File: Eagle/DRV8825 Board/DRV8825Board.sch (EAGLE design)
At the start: 10 parts, among them X1 22-23-2031, X2 22-23-2041, X3 22-23-2041

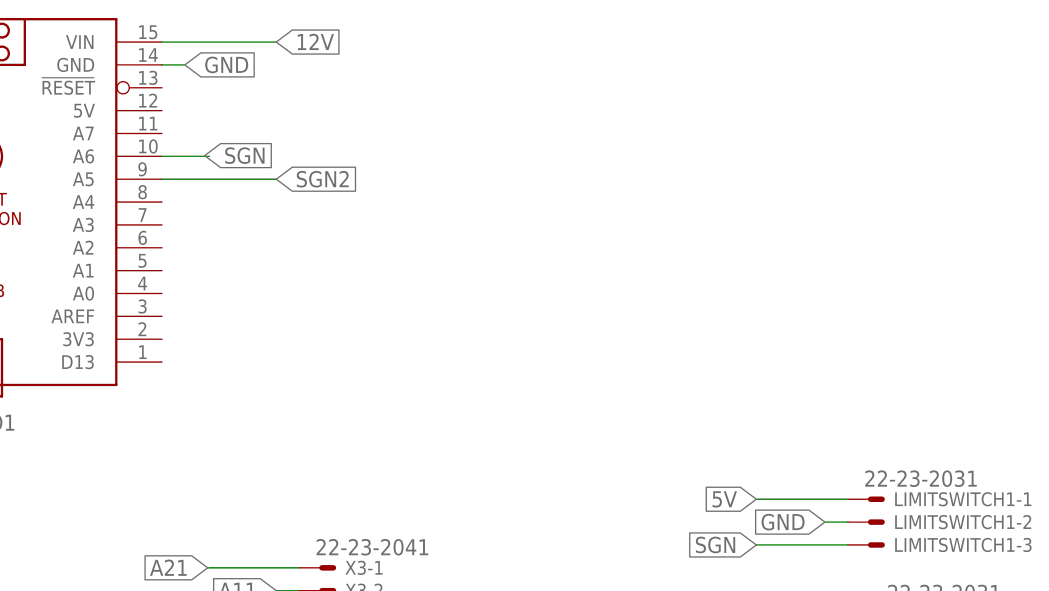
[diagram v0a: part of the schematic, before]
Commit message: Added a fan controller circuit
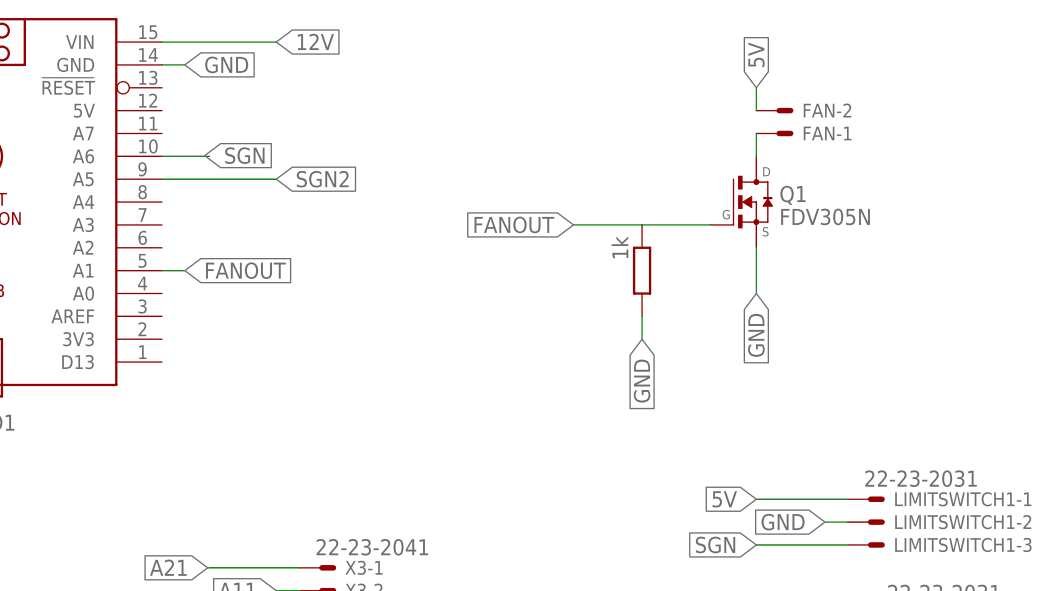
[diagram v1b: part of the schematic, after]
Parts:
- added FAN: 22-23-2021, con-molex:22-23-2021
- added Q1: FDV305N, FDV305N:FDV305N
- added R1: 1k, rcl:R-EU_R1206
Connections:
- new net FANOUT: ARDUINO_NANO1.A1, Q1.G, R1.1
- new net N$1: FAN-1.S, Q1.D
- net 5V: now also FAN-2.S
- net GND: now also Q1.S, R1.2
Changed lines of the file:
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@@
 <part name="C2" library="rcl" library_urn="urn:adsk.eagle:library:334" deviceset="CPOL-EU" device="E2.5-6" package3d_urn="urn:adsk.eagle:package:23349/1"/>
 <part name="X2" library="con-molex" library_urn="urn:adsk.eagle:library:165" deviceset="22-23-2041" device="" package3d_urn="urn:adsk.eagle:package:8078635/1"/>
+<part name="Q1" library="FDV305N" deviceset="FDV305N" device=""/>
+<part name="FAN" library="con-molex" library_urn="urn:adsk.eagle:library:165" deviceset="22-23-2021" device="" package3d_urn="urn:adsk.eagle:package:8078633/1"/>
+<part name="R1" library="rcl" library_urn="urn:adsk.eagle:library:334" deviceset="R-EU_" device="R1206" package3d_urn="urn:adsk.eagle:package:23540/2" value="1k"/>
 </parts>
 <sheets>
@@
 <attribute name="NAME" x="38.1" y="42.418" size="1.524" layer="95"/>
 </instance>
+<instance part="Q1" gate="G$1" x="83.82" y="139.7" smashed="yes">
+<attribute name="VALUE" x="86.36128125" y="137.15871875" size="1.778890625" layer="96"/>
+<attribute name="NAME" x="86.36438125" y="139.7" size="1.781059375" layer="95"/>
+</instance>
+<instance part="FAN" gate="-1" x="86.36" y="147.32" smashed="yes">
+<attribute name="NAME" x="88.9" y="146.558" size="1.524" layer="95"/>
+</instance>
+<instance part="FAN" gate="-2" x="86.36" y="149.86" smashed="yes">
+<attribute name="NAME" x="88.9" y="149.098" size="1.524" layer="95"/>
+</instance>
+<instance part="R1" gate="G$1" x="71.12" y="132.08" smashed="yes" rot="R270">
+<attribute name="VALUE" x="67.818" y="135.89" size="1.778" layer="96" rot="R270"/>
+</instance>
 </instances>
 <busses>
@@
 <wire x1="-68.58" y1="101.6" x2="-88.9" y2="101.6" width="0.1524" layer="91"/>
 <label x="-88.9" y="101.6" size="1.778" layer="95" rot="R180" xref="yes"/>
+</segment>
+<segment>
+<pinref part="FAN" gate="-2" pin="S"/>
+<wire x1="83.82" y1="149.86" x2="83.82" y2="152.4" width="0.1524" layer="91"/>
+<label x="83.82" y="152.4" size="1.778" layer="95" rot="R90" xref="yes"/>
 </segment>
 </net>
@@
 <wire x1="-12.7" y1="43.18" x2="-12.7" y2="33.02" width="0.1524" layer="91"/>
 </segment>
+<segment>
+<pinref part="Q1" gate="G$1" pin="S"/>
+<wire x1="83.82" y1="134.62" x2="83.82" y2="129.54" width="0.1524" layer="91"/>
+<label x="83.82" y="129.54" size="1.778" layer="95" rot="R270" xref="yes"/>
+</segment>
+<segment>
+<pinref part="R1" gate="G$1" pin="2"/>
+<wire x1="71.12" y1="127" x2="71.12" y2="124.46" width="0.1524" layer="91"/>
+<label x="71.12" y="124.46" size="1.778" layer="95" rot="R270" xref="yes"/>
+</segment>
 </net>
 <net name="12V" class="0">
@@
 </segment>
 </net>
+<net name="FANOUT" class="0">
+<segment>
+<pinref part="Q1" gate="G$1" pin="G"/>
+<pinref part="R1" gate="G$1" pin="1"/>
+<wire x1="78.74" y1="137.16" x2="71.12" y2="137.16" width="0.1524" layer="91"/>
+<wire x1="71.12" y1="137.16" x2="63.5" y2="137.16" width="0.1524" layer="91"/>
+<label x="63.5" y="137.16" size="1.778" layer="95" rot="R180" xref="yes"/>
+</segment>
+<segment>
+<pinref part="ARDUINO_NANO1" gate="G$1" pin="A1"/>
+<wire x1="17.78" y1="132.08" x2="20.32" y2="132.08" width="0.1524" layer="91"/>
+<label x="20.32" y="132.08" size="1.778" layer="95" xref="yes"/>
+</segment>
+</net>
+<net name="N$1" class="0">
+<segment>
+<pinref part="FAN" gate="-1" pin="S"/>
+<pinref part="Q1" gate="G$1" pin="D"/>
+<wire x1="83.82" y1="147.32" x2="83.82" y2="144.78" width="0.1524" layer="91"/>
+</segment>
+</net>

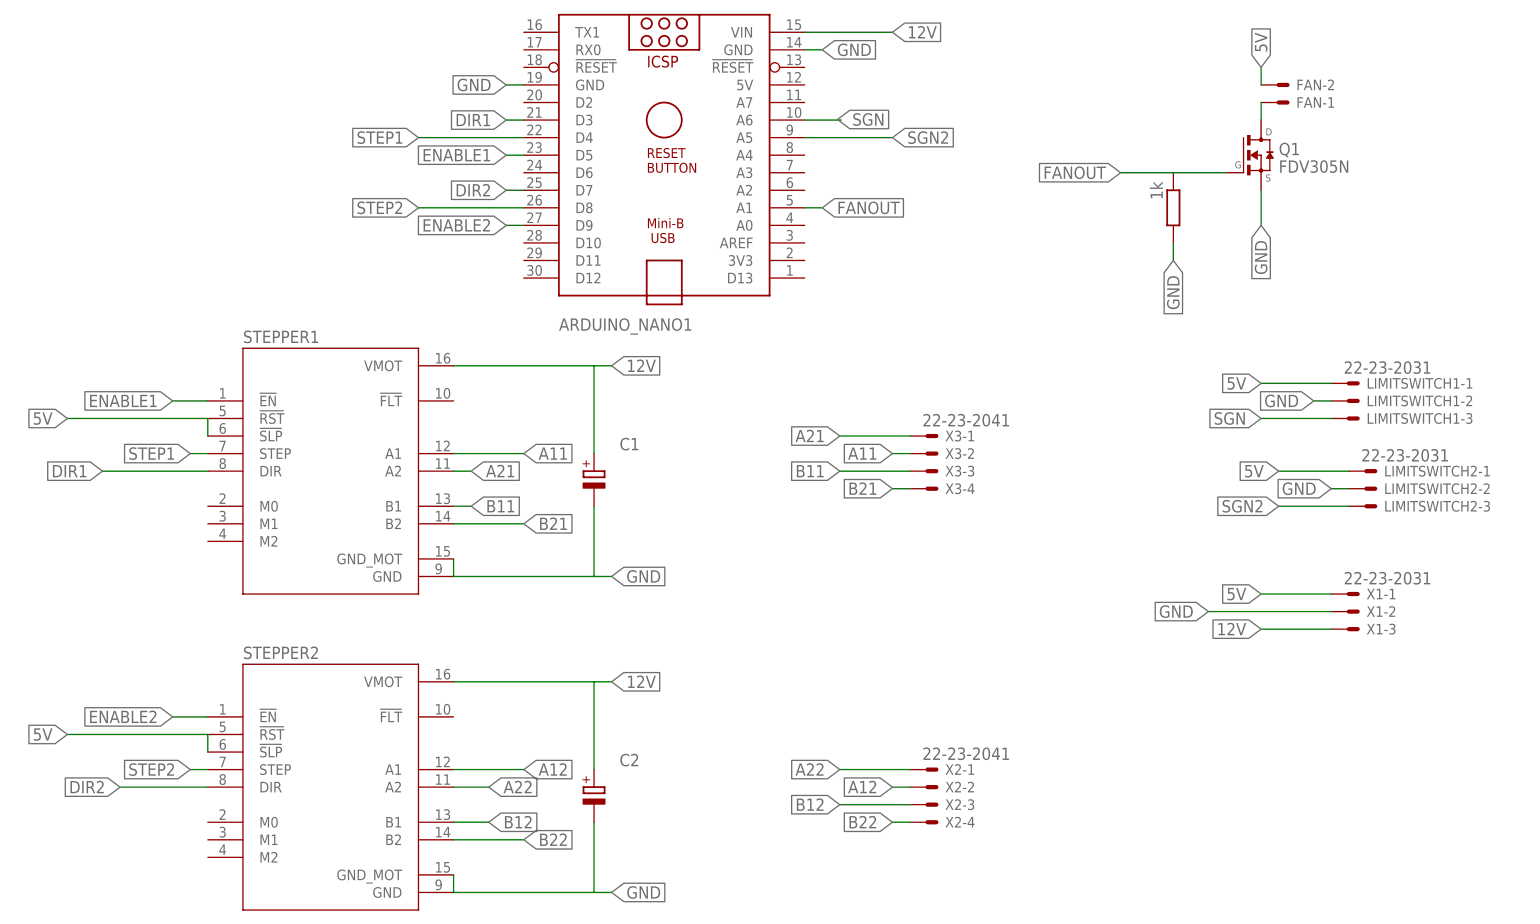
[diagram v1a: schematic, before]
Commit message: Updated to include all the limitswitches from the gripper
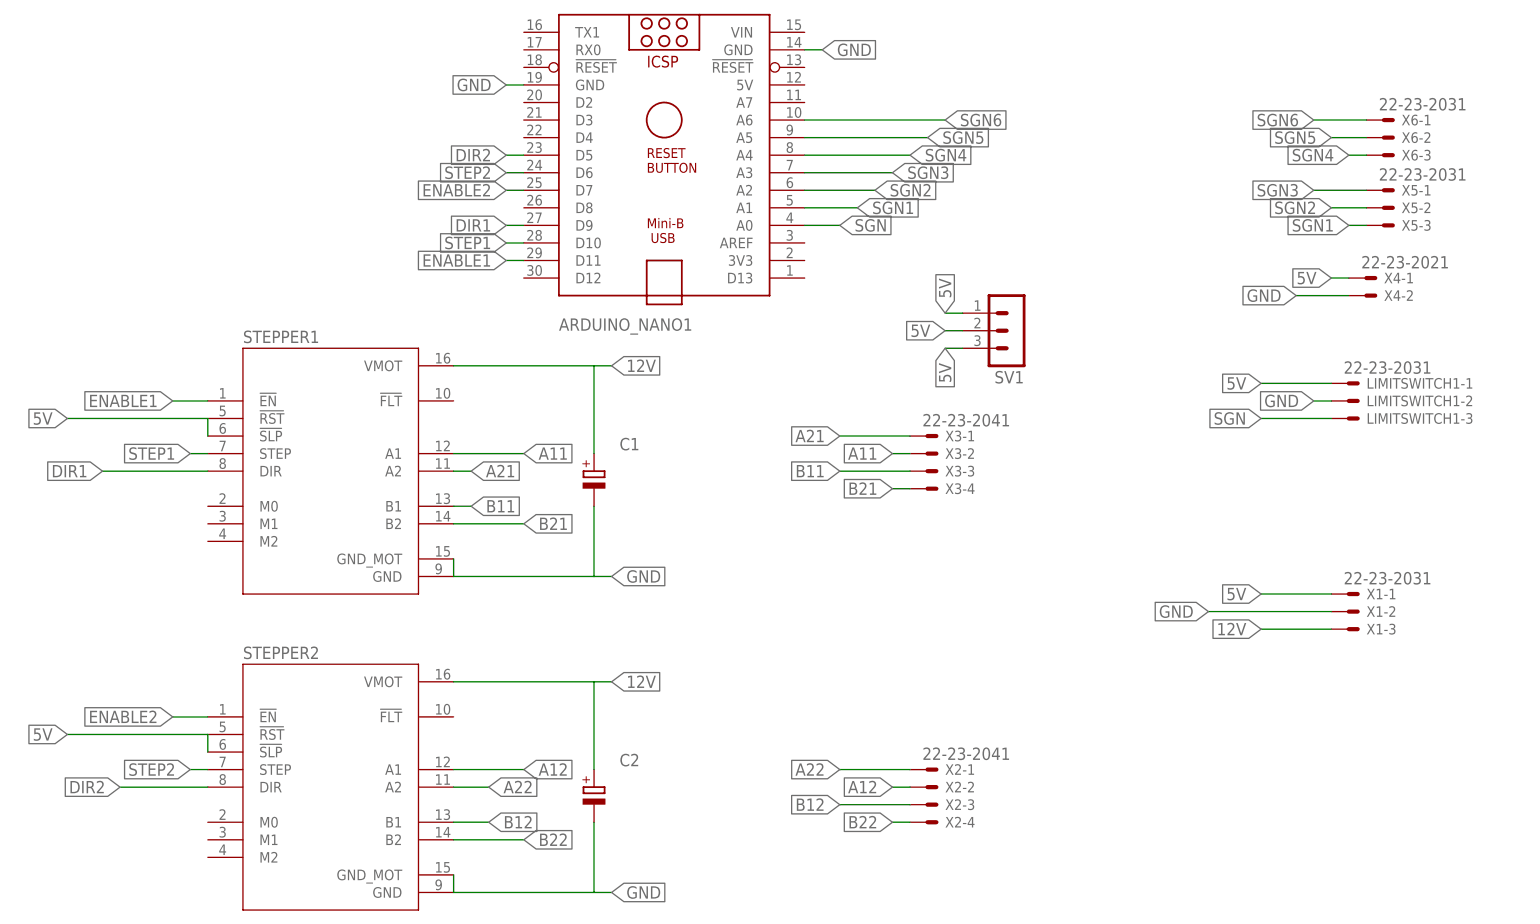
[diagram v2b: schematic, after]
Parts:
- removed FAN: 22-23-2021, con-molex:22-23-2021
- removed LIMITSWITCH2: 22-23-2031, con-molex:22-23-2031
- removed Q1: FDV305N, FDV305N:FDV305N
- removed R1: 1k, rcl:R-EU_R1206
- added SV1: (no value), con-lstb:MA03-1
- added X4: 22-23-2021, con-molex:22-23-2021
- added X5, X6: 22-23-2031, con-molex:22-23-2031
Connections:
- removed net FANOUT: ARDUINO_NANO1.A1, Q1.G, R1.1
- removed net N$1: FAN-1.S, Q1.D
- new net SGN1: ARDUINO_NANO1.A1, X5-3.S
- new net SGN3: ARDUINO_NANO1.A3, X5-1.S
- new net SGN4: ARDUINO_NANO1.A4, X6-3.S
- new net SGN5: ARDUINO_NANO1.A5, X6-2.S
- new net SGN6: ARDUINO_NANO1.A6, X6-1.S
- net 12V: no longer ARDUINO_NANO1.VIN
- net 5V: now also SV1.1, SV1.2, SV1.3, X4-1.S; no longer FAN-2.S, LIMITSWITCH2-1.S
- net DIR1: now also ARDUINO_NANO1.D9; no longer ARDUINO_NANO1.D3
- net DIR2: now also ARDUINO_NANO1.D5; no longer ARDUINO_NANO1.D7
- net ENABLE1: now also ARDUINO_NANO1.D11; no longer ARDUINO_NANO1.D5
- net ENABLE2: now also ARDUINO_NANO1.D7; no longer ARDUINO_NANO1.D9
- net GND: now also X4-2.S; no longer LIMITSWITCH2-2.S, Q1.S, R1.2
- net SGN: now also ARDUINO_NANO1.A0; no longer ARDUINO_NANO1.A6
- net SGN2: now also ARDUINO_NANO1.A2, X5-2.S; no longer ARDUINO_NANO1.A5, LIMITSWITCH2-3.S
- net STEP1: now also ARDUINO_NANO1.D10; no longer ARDUINO_NANO1.D4
- net STEP2: now also ARDUINO_NANO1.D6; no longer ARDUINO_NANO1.D8
